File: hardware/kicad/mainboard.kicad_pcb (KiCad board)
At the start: 4 copper layers, 151.8 x 109.6 mm, 83 parts, among them J1 XT60PW, J10 Body NeoPixel, J11 Slip ring, J12 Charger XT30, J13 SPK L, J14 SPK R, J15 ESTOP, J16 I2C-A exp (ESP32), J17 I2C-B exp (RP2350), J2 DFR0601 ribbon 2x5, J3 DFR0601 ribbon 2x5, J4 Servo L, J5 Servo R, J6 IMU BMI160 SPI, J7 S2S AS5600/pot, J8 Dome encoder, J9 Hall, Q1 SQJ431EP P-FET RPP, U1 ESP-WROOM-32 DevKit 30p, U2 RP2350-Zero, U3 DFPlayer Mini, U5 AP7361C-33 3.3V LDO, U6 74AHCT125, U7 74LVC245A

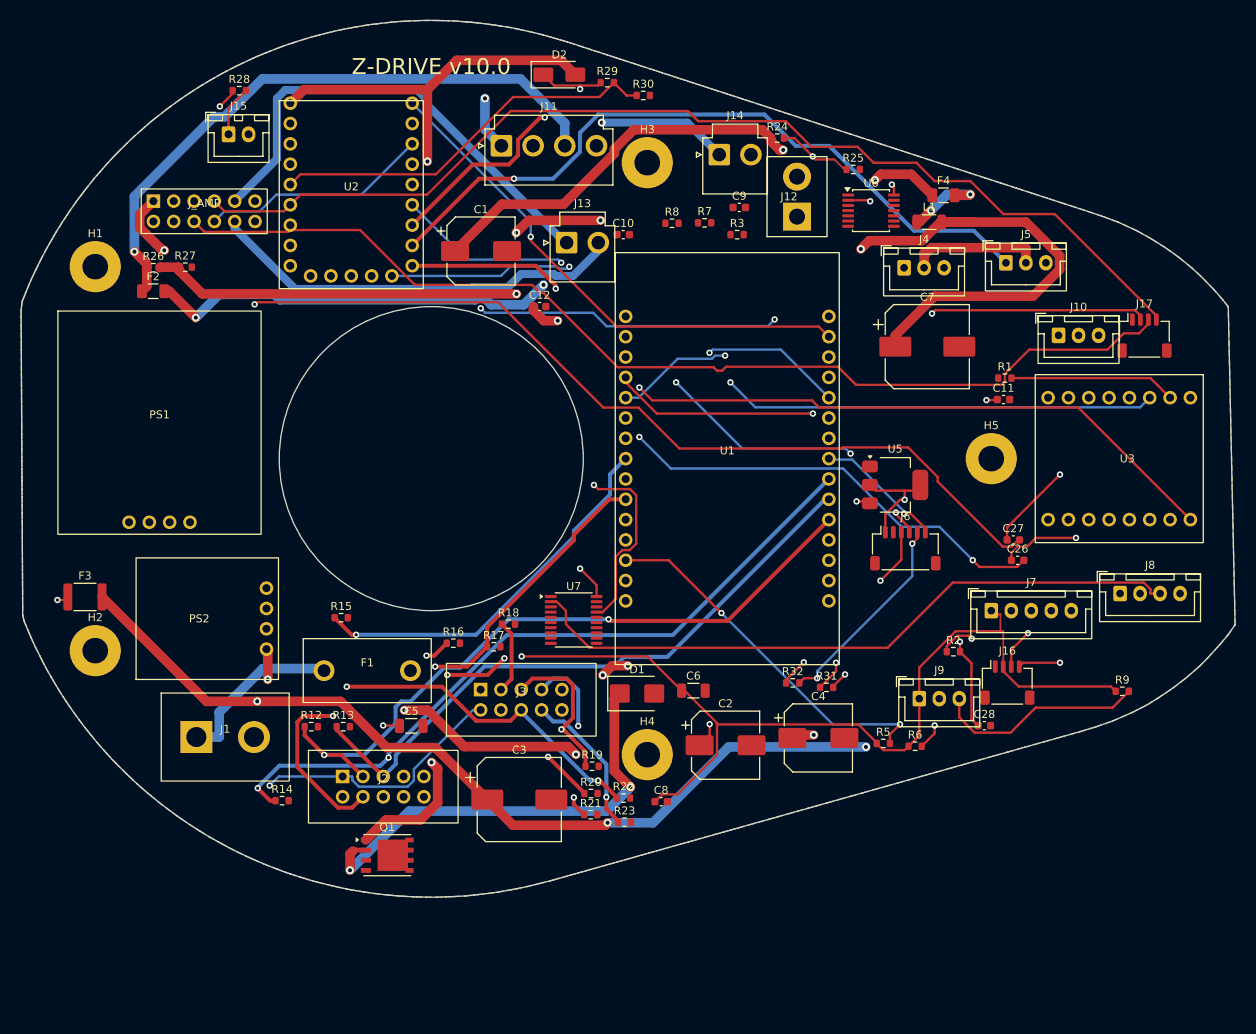
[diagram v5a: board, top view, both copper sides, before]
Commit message: v10.1 mainboard: casing extended 15mm down (top fixed), parts spaced 2.5x, DFPlayer SD-slot faces the tail (silk + card keepout); autoroute 12->5 signal opens; updated STEP/outline for Fusion
Co-Authored-By: Claude Opus 5 (1M context) <noreply@anthropic.com>
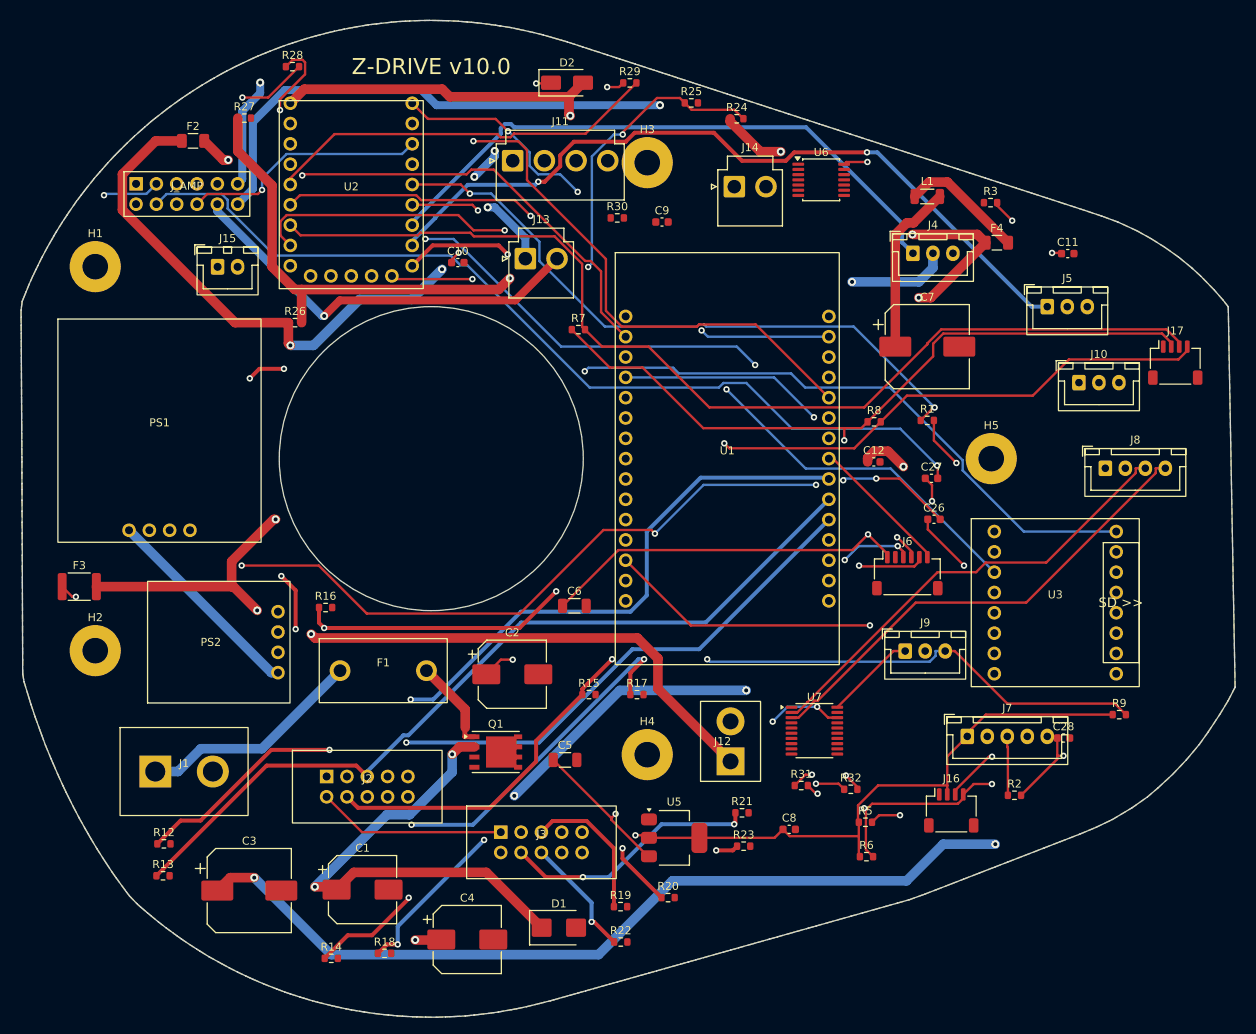
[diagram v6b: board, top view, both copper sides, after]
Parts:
- moved C1 81.2 mm to (141.4, 203.9)
- moved J12 68.6 mm to (187.4, 185.3)
- moved U5 52.1 mm to (180.4, 197.4)
- moved C4 50.6 mm to (154.5, 210.1)
- moved C12 46.1 mm to (205.3, 150.4)
- moved R18 44.0 mm to (144.2, 211.8)
- moved C3 35.6 mm to (127.2, 204.0)
- moved R8 35.4 mm to (205.4, 145.4)
- moved U7 33.1 mm to (197.9, 184.0)
- moved R15 32.4 mm to (169.7, 179.5)
- moved R3 31.9 mm to (219.9, 118.0)
- moved D1 30.9 mm to (165.9, 208.6)
- moved R13 29.2 mm to (116.5, 202.1)
- moved C2 28.1 mm to (160.1, 176.9)
- moved R12 23.5 mm to (116.6, 198.2)
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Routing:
- net AMP_12V: track 249.1 -> 21.6 mm, vias 6 -> 0
- net ENC_A_3V3: track 0.00 -> 114.2 mm, vias 0 -> 4
- net ESTOP_SENSE: track 6.36 -> 95.4 mm, vias 0 -> 2
- net NEO_3V3: track 87.2 -> 0.00 mm, vias 3 -> 0
- net DF_TX_RP: track 0.00 -> 80.9 mm, vias 0 -> 2
- net ENC_B_3V3: track 68.1 -> 0.00 mm, vias 1 -> 0
- net ENC_B_5V: track 0.00 -> 60.1 mm
- net +3V3: track 365.7 -> 417.2 mm, vias 6 -> 4
- net CHG_F: track 95.6 -> 146.4 mm, vias 4 -> 2
- net CHG-: track 28.7 -> 77.1 mm
- net RP_5V: track 78.3 -> 125.3 mm
- net FLY_PWM: track 50.0 -> 84.0 mm, vias 0 -> 2
- net AMP_INL: track 128.0 -> 160.3 mm, vias 2 -> 6
- net NEO_OUT: track 0.00 -> 29.5 mm, vias 0 -> 1
- net DOME_INB: track 111.4 -> 138.3 mm, vias 1 -> 5
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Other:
- board size 151.8 x 109.6 mm -> 151.8 x 124.6 mm
- board text added: "rev A 77e3840 2026-08-21"
- board text removed: "rev A 00f3452 2026-08-21"
